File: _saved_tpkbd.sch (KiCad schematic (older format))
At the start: 21 parts, among them CON1 AVR-ISP-6, J1 CONN_01X02, J2 CONN_01X01, J3 USB_OTG, J4 CONN_02X20, J5 CONN_01X04, J6 GS2, J7 0, U1 ATMEGA8515-16AU, U2 AP111733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

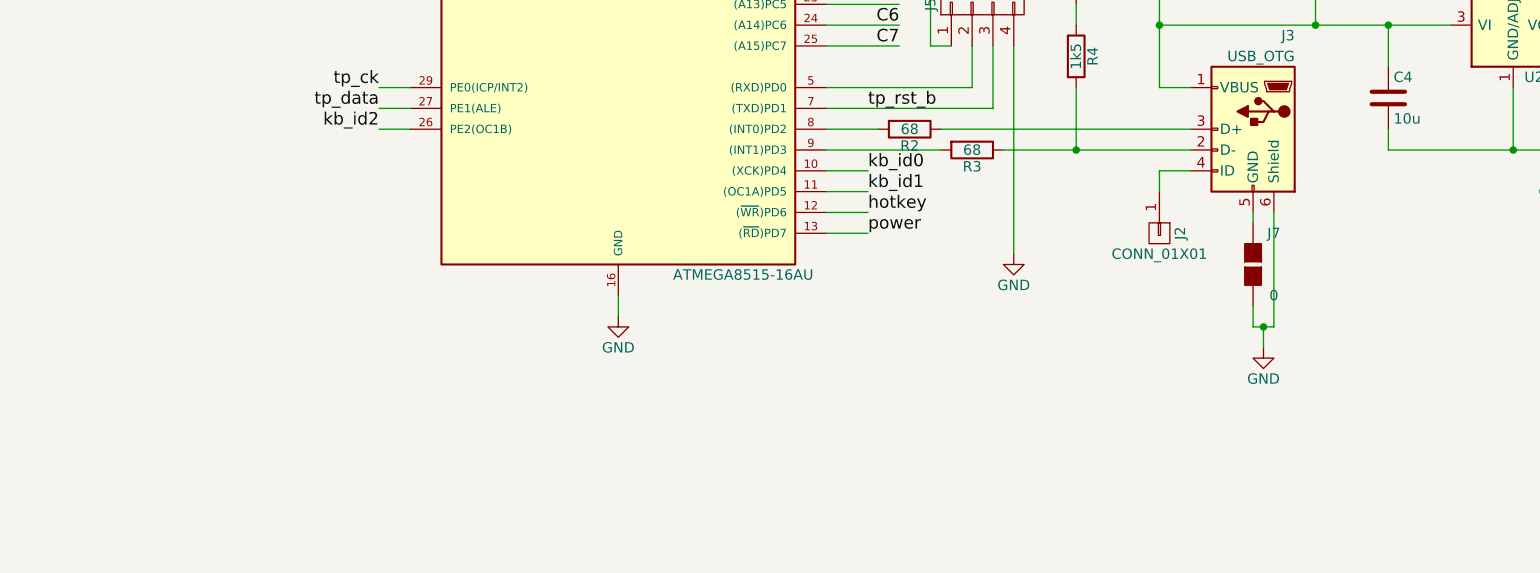
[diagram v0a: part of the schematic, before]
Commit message: added a LED
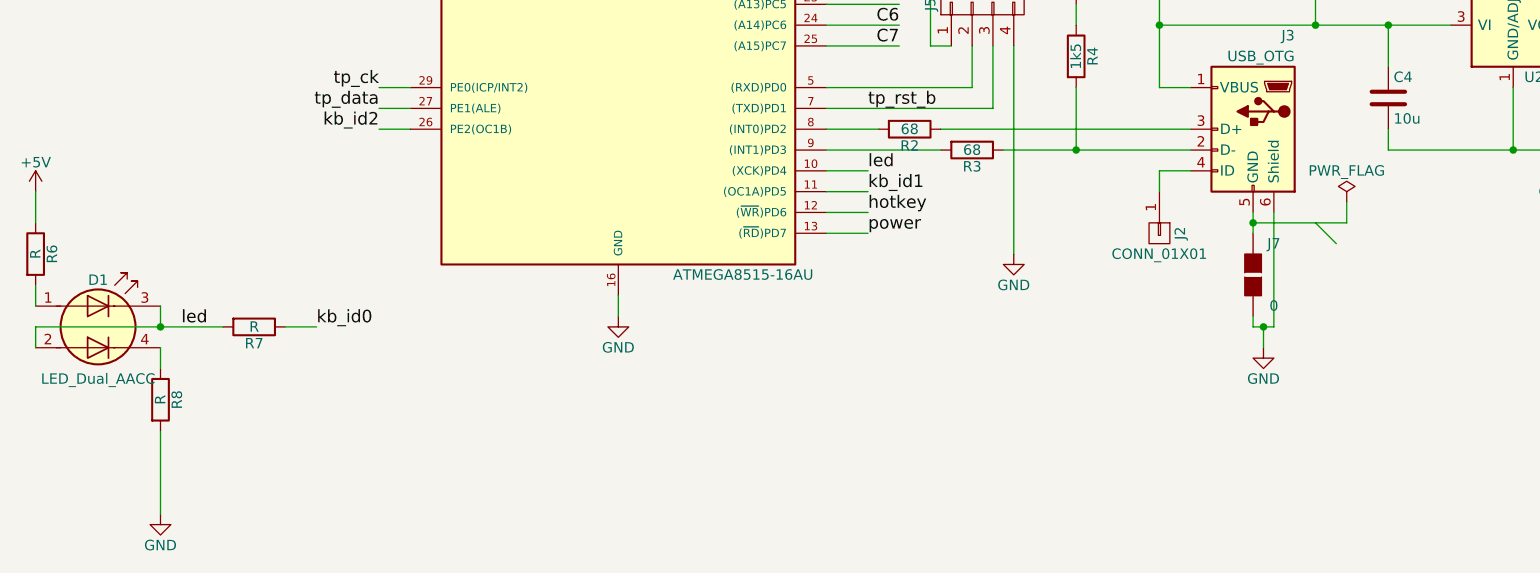
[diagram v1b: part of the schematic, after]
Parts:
- added D1: LED_Dual_AACC, symbol LED_Dual_AACC
- added R6, R7, R8: R, Resistors_SMD:R_0603_HandSoldering, symbol R
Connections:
- net +5V: now also R6.1
- net GND: now also R8.2
- net kb_id0: now also R7.1; no longer U1.10 ((XCK)PD4)
- new net: D1.1 (A1), R6.2
- new net: D1.4 (K2), R8.1
- new net led: D1.2 (A2), D1.3 (K1), R7.2, U1.10 ((XCK)PD4)
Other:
- moved on the sheet: J7
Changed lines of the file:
@@
 LIBS:contrib
 LIBS:valves
+LIBS:tpkbd-cache
 EELAYER 25 0
 EELAYER END
@@
 	6150 5700 6300 5700
 Wire Wire Line
-	6600 6350 6600 6450
-Wire Wire Line
 	6600 6450 6700 6450
 Wire Wire Line
@@
 Wire Wire Line
 	4750 5900 4550 5900
-Text Label 4750 5700 0    60   ~ 0
+Text Label 2100 6450 0    60   ~ 0
 kb_id0
 Wire Wire Line
@@
 L GS2 J7
 U 1 1 59BB22E9
-P 6600 6150
-F 0 "J7" H 6700 6300 50  0000 C CNN
-F 1 "0" H 6700 6001 50  0000 C CNN
-F 2 "Capacitors_SMD:C_0402" V 6674 6150 50  0001 C CNN
-F 3 "" H 6600 6150 50  0001 C CNN
-	1    6600 6150
-	1    0    0    -1
-$EndComp
-Wire Wire Line
-	6600 5900 6600 5950
+P 6600 6200
+F 0 "J7" H 6700 6350 50  0000 C CNN
+F 1 "0" H 6700 6051 50  0000 C CNN
+F 2 "Capacitors_SMD:C_0402" V 6674 6200 50  0001 C CNN
+F 3 "" H 6600 6200 50  0001 C CNN
+	1    6600 6200
+	1    0    0    -1
+$EndComp
+Wire Wire Line
+	6600 5900 6600 6000
+Text Label 4750 5700 0    60   ~ 0
+led
+Text Label 1450 6450 0    60   ~ 0
+led
+$Comp
+L R R6
+U 1 1 59BB2C23
+P 750 6100
+F 0 "R6" V 830 6100 50  0000 C CNN
+F 1 "R" V 750 6100 50  0000 C CNN
+F 2 "Resistors_SMD:R_0603_HandSoldering" V 680 6100 50  0001 C CNN
+F 3 "" H 750 6100 50  0001 C CNN
+	1    750  6100
+	1    0    0    -1
+$EndComp
+$Comp
+L +5V #PWR024
+U 1 1 59BB2C76
+P 750 5800
+F 0 "#PWR024" H 750 5650 50  0001 C CNN
+F 1 "+5V" H 750 5940 50  0000 C CNN
+F 2 "" H 750 5800 50  0001 C CNN
+F 3 "" H 750 5800 50  0001 C CNN
+	1    750  5800
+	1    0    0    -1
+$EndComp
+Wire Wire Line
+	750  5800 750  5950
+Wire Wire Line
+	750  6250 750  6350
+$Comp
+L GND #PWR025
+U 1 1 59BB2E4B
+P 1350 7350
+F 0 "#PWR025" H 1350 7100 50  0001 C CNN
+F 1 "GND" H 1350 7200 50  0000 C CNN
+F 2 "" H 1350 7350 50  0001 C CNN
+F 3 "" H 1350 7350 50  0001 C CNN
+	1    1350 7350
+	1    0    0    -1
+$EndComp
+Wire Wire Line
+	1350 6950 1350 7350
+$Comp
+L PWR_FLAG #FLG026
+U 1 1 59BB3276
+P 7050 5850
+F 0 "#FLG026" H 7050 5925 50  0001 C CNN
+F 1 "PWR_FLAG" H 7050 6000 50  0000 C CNN
+F 2 "" H 7050 5850 50  0001 C CNN
+F 3 "" H 7050 5850 50  0001 C CNN
+	1    7050 5850
+	1    0    0    -1
+$EndComp
+Wire Wire Line
+	6600 5950 7050 5950
+Wire Wire Line
+	7050 5950 7050 5850
+Entry Wire Line
+	6900 5950 7000 6050
+Connection ~ 6600 5950
+Wire Wire Line
+	6600 6400 6600 6450
+$Comp
+L R R7
+U 1 1 59BB3743
+P 1800 6450
+F 0 "R7" V 1880 6450 50  0000 C CNN
+F 1 "R" V 1800 6450 50  0000 C CNN
+F 2 "Resistors_SMD:R_0603_HandSoldering" V 1730 6450 50  0001 C CNN
+F 3 "" H 1800 6450 50  0001 C CNN
+	1    1800 6450
+	0    1    1    0
+$EndComp
+Wire Wire Line
+	1950 6450 2100 6450
+$Comp
+L R R8
+U 1 1 59BB3CEE
+P 1350 6800
+F 0 "R8" V 1430 6800 50  0000 C CNN
+F 1 "R" V 1350 6800 50  0000 C CNN
+F 2 "Resistors_SMD:R_0603_HandSoldering" V 1280 6800 50  0001 C CNN
+F 3 "" H 1350 6800 50  0001 C CNN
+	1    1350 6800
+	1    0    0    -1
+$EndComp
+Wire Wire Line
+	1350 6550 1350 6650
+$Comp
+L LED_Dual_AACC D1
+U 1 1 59BB3F41
+P 1050 6450
+F 0 "D1" H 1050 6675 50  0000 C CNN
+F 1 "LED_Dual_AACC" H 1050 6200 50  0000 C CNN
+F 2 "" H 1080 6450 50  0001 C CNN
+F 3 "" H 1080 6450 50  0001 C CNN
+	1    1050 6450
+	1    0    0    -1
+$EndComp
+Wire Wire Line
+	750  6450 1650 6450
+Wire Wire Line
+	750  6450 750  6550
+Wire Wire Line
+	1350 6350 1350 6450
+Connection ~ 1350 6450
 $EndSCHEMATC

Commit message: cleanup
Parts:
- removed CON1: AVR-ISP-6, Pin_Headers:Pin_Header_Straight_2x03, symbol AVR-ISP-6
- added J8: CONN_01X06, Pin_Headers:Pin_Header_Straight_1x06, symbol CONN_01X06
- C1, C2: footprint Capacitors_SMD:C_0805_HandSoldering -> Capacitors_SMD:C_0603_HandSoldering
- C3: footprint Capacitors_SMD:C_0402 -> Capacitors_SMD:C_0603_HandSoldering
- D1: value LED_Dual_AACC -> LED; footprint (none) -> KX14:PLCC4
- J2: footprint Pin_Headers:Pin_Header_Straight_1x01 -> KX14:Pins1x1
- J4: value CONN_02X20 -> CONN_02X21; symbol CONN_02X20 -> CONN_02X21
- R1, R2, R3, R4, R5: footprint Resistors_SMD:R_0805_HandSoldering -> Resistors_SMD:R_0603_HandSoldering
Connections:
- wire segments 152 -> 154
- no-connect marks 4 -> 5
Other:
- moved on the sheet: D1, R3
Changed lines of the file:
@@
 F 0 "C1" H 1625 3200 50  0000 L CNN
 F 1 "C" H 1625 3000 50  0000 L CNN
-F 2 "Capacitors_SMD:C_0805_HandSoldering" H 1638 2950 50  0001 C CNN
+F 2 "Capacitors_SMD:C_0603_HandSoldering" H 1638 2950 50  0001 C CNN
 F 3 "" H 1600 3100 50  0001 C CNN
 	1    1600 3100
@@
 F 0 "C2" H 1625 3600 50  0000 L CNN
 F 1 "C" H 1625 3400 50  0000 L CNN
-F 2 "Capacitors_SMD:C_0805_HandSoldering" H 1638 3350 50  0001 C CNN
+F 2 "Capacitors_SMD:C_0603_HandSoldering" H 1638 3350 50  0001 C CNN
 F 3 "" H 1600 3500 50  0001 C CNN
 	1    1600 3500
@@
 F 0 "R2" V 5030 5500 50  0000 C CNN
 F 1 "68" V 4950 5500 50  0000 C CNN
-F 2 "Resistors_SMD:R_0805_HandSoldering" V 4880 5500 50  0001 C CNN
+F 2 "Resistors_SMD:R_0603_HandSoldering" V 4880 5500 50  0001 C CNN
 F 3 "" H 4950 5500 50  0001 C CNN
 	1    4950 5500
@@
 L R R3
 U 1 1 59BAA9CB
-P 5250 5600
-F 0 "R3" V 5330 5600 50  0000 C CNN
-F 1 "68" V 5250 5600 50  0000 C CNN
-F 2 "Resistors_SMD:R_0805_HandSoldering" V 5180 5600 50  0001 C CNN
-F 3 "" H 5250 5600 50  0001 C CNN
-	1    5250 5600
+P 5200 5700
+F 0 "R3" V 5280 5700 50  0000 C CNN
+F 1 "68" V 5200 5700 50  0000 C CNN
+F 2 "Resistors_SMD:R_0603_HandSoldering" V 5130 5700 50  0001 C CNN
+F 3 "" H 5200 5700 50  0001 C CNN
+	1    5200 5700
 	0    1    1    0
 $EndComp
@@
 F 0 "J2" H 6150 6100 50  0000 C CNN
 F 1 "CONN_01X01" V 6250 6000 50  0000 C CNN
-F 2 "Pin_Headers:Pin_Header_Straight_1x01" H 6150 6000 50  0001 C CNN
+F 2 "KX14:Pins1x1" H 6150 6000 50  0001 C CNN
 F 3 "" H 6150 6000 50  0001 C CNN
 	1    6150 6000
@@
 F 0 "R1" V 2380 2350 50  0000 C CNN
 F 1 "10k" V 2300 2350 50  0000 C CNN
-F 2 "Resistors_SMD:R_0805_HandSoldering" V 2230 2350 50  0001 C CNN
+F 2 "Resistors_SMD:R_0603_HandSoldering" V 2230 2350 50  0001 C CNN
 F 3 "" H 2300 2350 50  0001 C CNN
 	1    2300 2350
@@
 F 0 "R4" V 5830 5150 50  0000 C CNN
 F 1 "1k5" V 5750 5150 50  0000 C CNN
-F 2 "Resistors_SMD:R_0805_HandSoldering" V 5680 5150 50  0001 C CNN
+F 2 "Resistors_SMD:R_0603_HandSoldering" V 5680 5150 50  0001 C CNN
 F 3 "" H 5750 5150 50  0001 C CNN
 	1    5750 5150
@@
 F 0 "C3" H 4125 1950 50  0000 L CNN
 F 1 "10n" H 4125 1750 50  0000 L CNN
-F 2 "Capacitors_SMD:C_0402" H 4138 1700 50  0001 C CNN
+F 2 "Capacitors_SMD:C_0603_HandSoldering" H 4138 1700 50  0001 C CNN
 F 3 "" H 4100 1850 50  0001 C CNN
 	1    4100 1850
@@
 $EndComp
 $Comp
-L CONN_02X20 J4
+L CONN_02X21 J4
 U 1 1 59BABC9C
-P 7600 2650
-F 0 "J4" H 7600 3700 50  0000 C CNN
-F 1 "CONN_02X20" V 7600 2650 50  0000 C CNN
-F 2 "KX14:KX14" H 7600 1700 50  0001 C CNN
-F 3 "" H 7600 1700 50  0001 C CNN
-	1    7600 2650
+P 7600 2700
+F 0 "J4" H 7600 3750 50  0000 C CNN
+F 1 "CONN_02X21" V 7600 2700 50  0000 C CNN
+F 2 "KX14:KX14" H 7600 1750 50  0001 C CNN
+F 3 "" H 7600 1750 50  0001 C CNN
+	1    7600 2700
 	1    0    0    -1
 $EndComp
@@
 	1    0    0    -1
 $EndComp
-$Comp
-L AVR-ISP-6 CON1
-U 1 1 59BABE2B
-P 5650 1950
-F 0 "CON1" H 5545 2190 50  0000 C CNN
-F 1 "AVR-ISP-6" H 5385 1720 50  0000 L BNN
-F 2 "Pin_Headers:Pin_Header_Straight_2x03" V 5130 1990 50  0001 C CNN
-F 3 "" H 5625 1950 50  0001 C CNN
-	1    5650 1950
-	1    0    0    -1
-$EndComp
 Text Label 2400 2600 0    60   ~ 0
 RST
-Text Label 5050 2050 0    60   ~ 0
+Text Label 10550 3050 2    60   ~ 0
 RST
 Text Label 7050 2500 0    60   ~ 0
@@
 	4550 5500 4800 5500
 Wire Wire Line
-	4550 5600 5100 5600
-Wire Wire Line
 	5100 5500 6300 5500
-Wire Wire Line
-	5400 5600 6300 5600
 Wire Wire Line
 	6150 5800 6150 5700
@@
 	5750 4900 5750 5000
 Wire Wire Line
-	5750 5300 5750 5600
+	5750 5300 5750 5700
 Connection ~ 5750 5600
 Wire Wire Line
@@
 Connection ~ 6150 5000
 Wire Wire Line
-	5050 2050 5500 2050
-Wire Wire Line
-	5050 1850 5500 1850
-Wire Wire Line
-	5050 1950 5500 1950
-Wire Wire Line
-	5750 1850 6200 1850
-Wire Wire Line
-	5750 1950 6200 1950
-Wire Wire Line
-	5750 2050 6200 2050
+	10550 3050 10100 3050
+Wire Wire Line
+	10550 2850 10100 2850
+Wire Wire Line
+	10550 2950 10100 2950
+Wire Wire Line
+	10100 2650 10550 2650
+Wire Wire Line
+	10100 2750 10550 2750
+Wire Wire Line
+	10100 3150 10550 3150
 Wire Wire Line
 	7350 2500 7050 2500
@@
 F 0 "R5" V 6730 3350 50  0000 C CNN
 F 1 "10k" V 6650 3350 50  0000 C CNN
-F 2 "Resistors_SMD:R_0805_HandSoldering" V 6580 3350 50  0001 C CNN
+F 2 "Resistors_SMD:R_0603_HandSoldering" V 6580 3350 50  0001 C CNN
 F 3 "" H 6650 3350 50  0001 C CNN
 	1    6650 3350
@@
 Wire Wire Line
 	4550 5100 4900 5100
-Text Label 5050 1850 0    60   ~ 0
+Text Label 10550 2850 2    60   ~ 0
 MISO
-Text Label 5050 1950 0    60   ~ 0
+Text Label 10550 2950 2    60   ~ 0
 SCK
-Text Label 6200 1950 0    60   ~ 0
+Text Label 10550 2750 0    60   ~ 0
 MOSI
 $Comp
 L GND #PWR014
 U 1 1 59BAD155
-P 6200 2150
-F 0 "#PWR014" H 6200 1900 50  0001 C CNN
-F 1 "GND" H 6200 2000 50  0000 C CNN
-F 2 "" H 6200 2150 50  0001 C CNN
-F 3 "" H 6200 2150 50  0001 C CNN
-	1    6200 2150
-	1    0    0    -1
-$EndComp
-Wire Wire Line
-	6200 2050 6200 2150
+P 10550 3250
+F 0 "#PWR014" H 10550 3000 50  0001 C CNN
+F 1 "GND" H 10550 3100 50  0000 C CNN
+F 2 "" H 10550 3250 50  0001 C CNN
+F 3 "" H 10550 3250 50  0001 C CNN
+	1    10550 3250
+	1    0    0    -1
+$EndComp
+Wire Wire Line
+	10550 3150 10550 3250
 Text Label 5100 4100 0    60   ~ 0
 MISO
@@
 	6900 4850 6900 5000
 Connection ~ 6900 5000
-$Comp
-L +3V3 #PWR017
-U 1 1 59BADCC0
-P 6200 1700
-F 0 "#PWR017" H 6200 1550 50  0001 C CNN
-F 1 "+3V3" H 6200 1840 50  0000 C CNN
-F 2 "" H 6200 1700 50  0001 C CNN
-F 3 "" H 6200 1700 50  0001 C CNN
-	1    6200 1700
-	1    0    0    -1
-$EndComp
-Wire Wire Line
-	6200 1850 6200 1700
+Wire Wire Line
+	10550 2650 10550 2500
 Wire Wire Line
 	4100 2200 4100 2000
@@
 tp_data
 Wire Wire Line
-	4750 5700 4550 5700
+	4750 5600 4550 5600
 $Comp
 L CONN_01X04 J5
@@
 	5350 5400 5350 5100
 $Comp
-L GND #PWR018
+L GND #PWR017
 U 1 1 59BAE839
 P 5450 6100
-F 0 "#PWR018" H 5450 5850 50  0001 C CNN
+F 0 "#PWR017" H 5450 5850 50  0001 C CNN
 F 1 "GND" H 5450 5950 50  0000 C CNN
 F 2 "" H 5450 6100 50  0001 C CNN
@@
 Wire Wire Line
 	5450 5100 5450 6100
-$Comp
-L +3V3 #PWR019
-U 1 1 59BAE923
-P 5050 4700
-F 0 "#PWR019" H 5050 4550 50  0001 C CNN
-F 1 "+3V3" H 5050 4840 50  0000 C CNN
-F 2 "" H 5050 4700 50  0001 C CNN
-F 3 "" H 5050 4700 50  0001 C CNN
-	1    5050 4700
-	1    0    0    -1
-$EndComp
 Wire Wire Line
 	5050 4700 5050 5100
@@
 	5050 5100 5150 5100
 $Comp
-L PWR_FLAG #FLG020
+L PWR_FLAG #FLG018
 U 1 1 59BAEACE
 P 9100 5450
-F 0 "#FLG020" H 9100 5525 50  0001 C CNN
+F 0 "#FLG018" H 9100 5525 50  0001 C CNN
 F 1 "PWR_FLAG" H 9100 5600 50  0000 C CNN
 F 2 "" H 9100 5450 50  0001 C CNN
@@
 Connection ~ 8500 5600
 $Comp
-L PWR_FLAG #FLG021
+L PWR_FLAG #FLG019
 U 1 1 59BAEC2F
 P 9450 4900
-F 0 "#FLG021" H 9450 4975 50  0001 C CNN
+F 0 "#FLG019" H 9450 4975 50  0001 C CNN
 F 1 "PWR_FLAG" H 9450 5050 50  0000 C CNN
 F 2 "" H 9450 4900 50  0001 C CNN
@@
 $EndComp
 $Comp
-L GND #PWR022
+L GND #PWR020
 U 1 1 59BAF57F
 P 1850 3800
-F 0 "#PWR022" H 1850 3550 50  0001 C CNN
+F 0 "#PWR020" H 1850 3550 50  0001 C CNN
 F 1 "GND" H 1850 3650 50  0000 C CNN
 F 2 "" H 1850 3800 50  0001 C CNN
@@
 	1850 3300 1900 3300
 $Comp
-L GND #PWR023
+L GND #PWR021
 U 1 1 59BAF671
 P 2350 3800
-F 0 "#PWR023" H 2350 3550 50  0001 C CNN
+F 0 "#PWR021" H 2350 3550 50  0001 C CNN
 F 1 "GND" H 2350 3650 50  0000 C CNN
 F 2 "" H 2350 3800 50  0001 C CNN
@@
 Wire Wire Line
 	6600 5900 6600 6000
-Text Label 4750 5700 0    60   ~ 0
+Text Label 4750 5600 0    60   ~ 0
 led
 Text Label 1450 6450 0    60   ~ 0
@@
 	1    0    0    -1
 $EndComp
-$Comp
-L +5V #PWR024
-U 1 1 59BB2C76
-P 750 5800
-F 0 "#PWR024" H 750 5650 50  0001 C CNN
-F 1 "+5V" H 750 5940 50  0000 C CNN
-F 2 "" H 750 5800 50  0001 C CNN
-F 3 "" H 750 5800 50  0001 C CNN
-	1    750  5800
-	1    0    0    -1
-$EndComp
 Wire Wire Line
 	750  5800 750  5950
@@
 	750  6250 750  6350
 $Comp
-L GND #PWR025
+L GND #PWR022
 U 1 1 59BB2E4B
 P 1350 7350
-F 0 "#PWR025" H 1350 7100 50  0001 C CNN
+F 0 "#PWR022" H 1350 7100 50  0001 C CNN
 F 1 "GND" H 1350 7200 50  0000 C CNN
 F 2 "" H 1350 7350 50  0001 C CNN
@@
 	1350 6950 1350 7350
 $Comp
-L PWR_FLAG #FLG026
+L PWR_FLAG #FLG023
 U 1 1 59BB3276
 P 7050 5850
-F 0 "#FLG026" H 7050 5925 50  0001 C CNN
+F 0 "#FLG023" H 7050 5925 50  0001 C CNN
 F 1 "PWR_FLAG" H 7050 6000 50  0000 C CNN
 F 2 "" H 7050 5850 50  0001 C CNN
@@
 P 1050 6450
 F 0 "D1" H 1050 6675 50  0000 C CNN
-F 1 "LED_Dual_AACC" H 1050 6200 50  0000 C CNN
-F 2 "" H 1080 6450 50  0001 C CNN
+F 1 "LED" H 1050 6200 50  0000 C CNN
+F 2 "KX14:PLCC4" H 1080 6450 50  0001 C CNN
 F 3 "" H 1080 6450 50  0001 C CNN
 	1    1050 6450
-	1    0    0    -1
+	1    0    0    1
 $EndComp
 Wire Wire Line
@@
 	1350 6350 1350 6450
 Connection ~ 1350 6450
+Wire Wire Line
+	4550 5700 5050 5700
+Wire Wire Line
+	5750 5700 5350 5700
+Wire Wire Line
+	5750 5600 6300 5600
+Wire Wire Line
+	7350 3700 7050 3700
+Connection ~ 7050 3700
+NoConn ~ 7850 3700
+$Comp
+L +3V3 #PWR024
+U 1 1 59BBC4D0
+P 750 5800
+F 0 "#PWR024" H 750 5650 50  0001 C CNN
+F 1 "+3V3" H 750 5940 50  0000 C CNN
+F 2 "" H 750 5800 50  0001 C CNN
+F 3 "" H 750 5800 50  0001 C CNN
+	1    750  5800
+	1    0    0    -1
+$EndComp
+$Comp
+L +5V #PWR025
+U 1 1 59BBCA91
+P 5050 4700
+F 0 "#PWR025" H 5050 4550 50  0001 C CNN
+F 1 "+5V" H 5050 4840 50  0000 C CNN
+F 2 "" H 5050 4700 50  0001 C CNN
+F 3 "" H 5050 4700 50  0001 C CNN
+	1    5050 4700
+	1    0    0    -1
+$EndComp
+$Comp
+L CONN_01X06 J8
+U 1 1 59BBF4F8
+P 9900 2900
+F 0 "J8" H 9900 3250 50  0000 C CNN
+F 1 "CONN_01X06" V 10000 2900 50  0000 C CNN
+F 2 "Pin_Headers:Pin_Header_Straight_1x06" H 9900 2900 50  0001 C CNN
+F 3 "" H 9900 2900 50  0001 C CNN
+	1    9900 2900
+	-1   0    0    1
+$EndComp
+$Comp
+L +5V #PWR026
+U 1 1 59BBF8A8
+P 10550 2500
+F 0 "#PWR026" H 10550 2350 50  0001 C CNN
+F 1 "+5V" H 10550 2640 50  0000 C CNN
+F 2 "" H 10550 2500 50  0001 C CNN
+F 3 "" H 10550 2500 50  0001 C CNN
+	1    10550 2500
+	1    0    0    -1
+$EndComp
 $EndSCHEMATC
